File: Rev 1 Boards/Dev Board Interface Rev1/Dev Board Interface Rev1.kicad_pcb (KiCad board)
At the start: 2 copper layers, 53 x 45 mm, 25 parts, among them J1 Conn_01x02_Pin, J2 Conn_01x02_Pin, J3 Conn_01x04_Pin, U1 TLV9301xDBV, U2 ADS1014IDGS, U3 ADS1014IDGS, U4 ISO164xB, U5 DACx53401

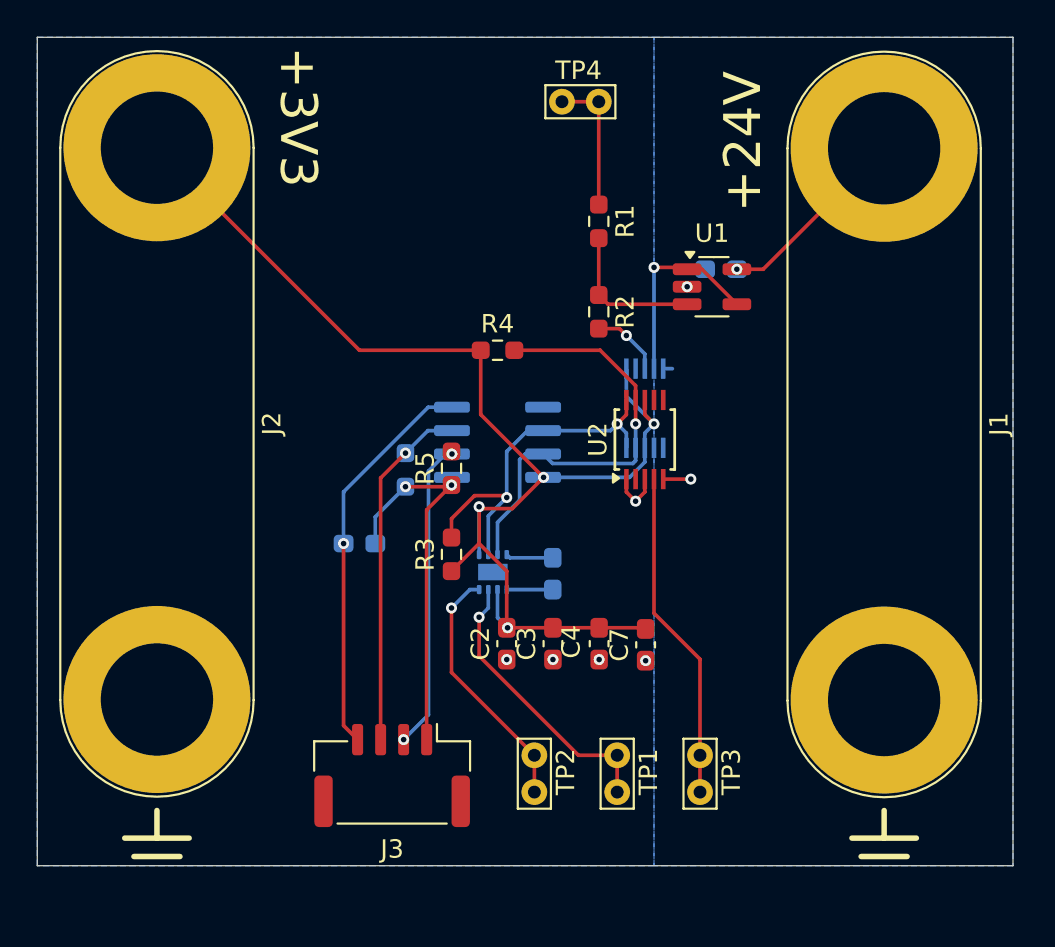
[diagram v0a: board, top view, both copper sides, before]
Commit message: implemented dev board interface review suggestions as per morris
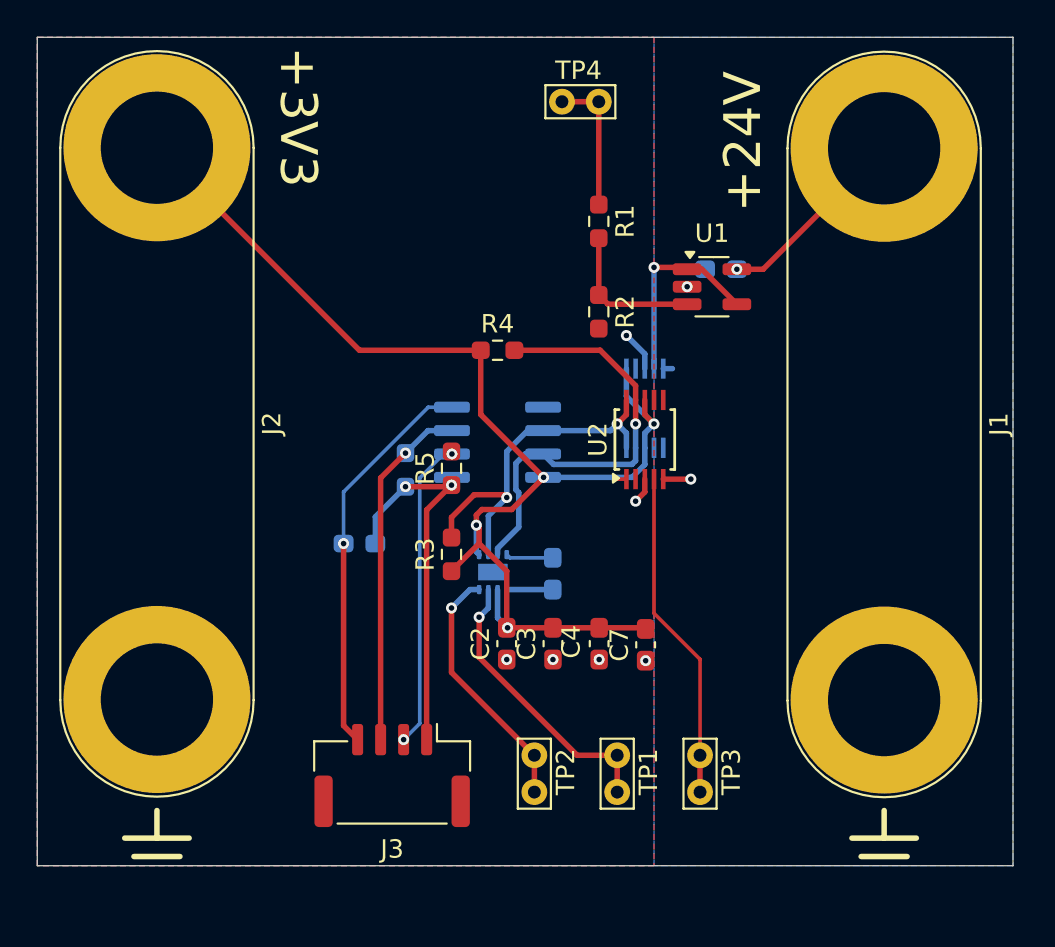
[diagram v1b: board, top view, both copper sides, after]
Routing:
- net GND: track 9.18 -> 6.62 mm
- net +3V3: track 69.9 -> 68.9 mm
- added copper zone on F.Cu, net GND

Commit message: Did partial fixes according to round 2 review of dev board interface as per jed
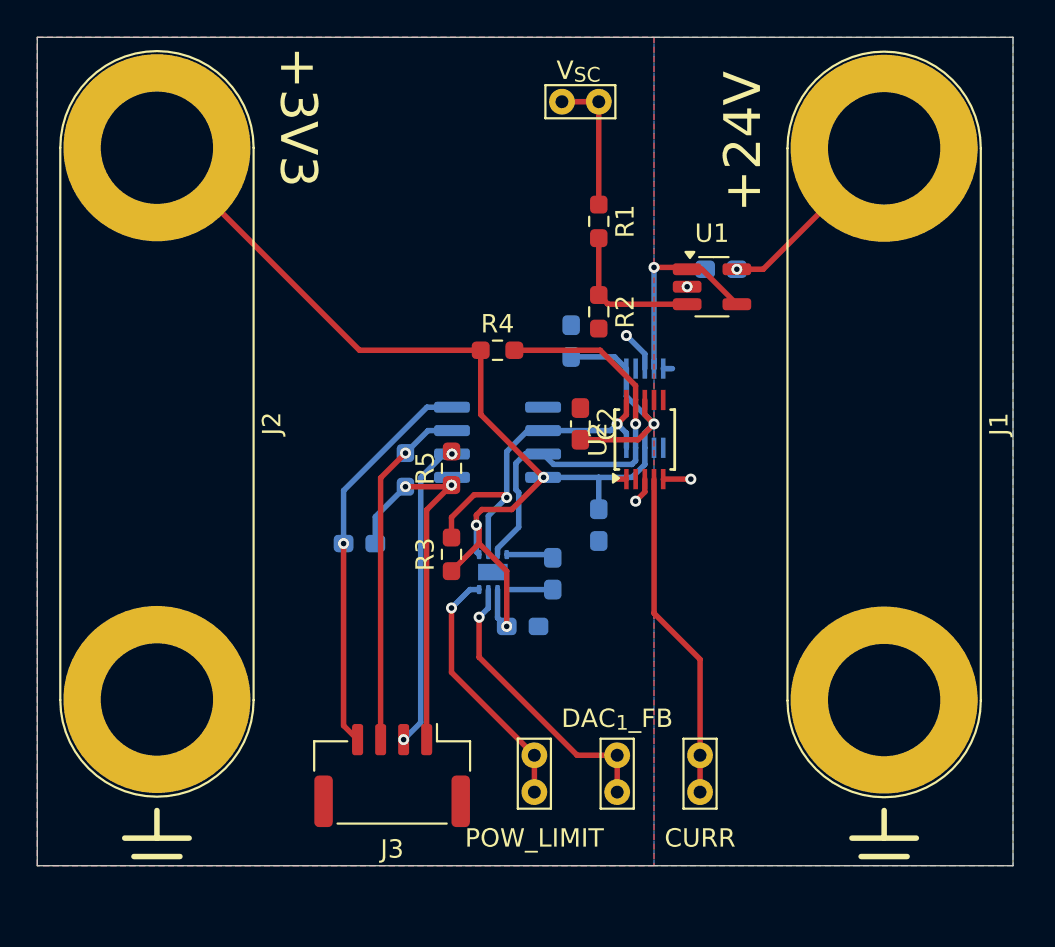
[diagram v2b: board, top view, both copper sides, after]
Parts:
- C3, C4, C7: moved to B.Cu
- moved C3 16.5 mm to (80.0, 106.0), turned to -90 degrees
- moved C2 12.6 mm to (80.5, 110.5), turned to -90 degrees
- moved C7 6.76 mm to (77.4, 121.5), turned to 180 degrees
- moved C4 6.44 mm to (81.5, 116.0)
- renumbered TP3 to CURR, TP1 to DAC_{1}_FB, TP2 to POW_LIMIT, TP4 to V_{SC}
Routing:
- net +3V3: track 68.9 -> 70.5 mm
- net GND: vias 6 -> 2

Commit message: reworked dev board interface pcb layout to put all ICs on the same side as  per jed review
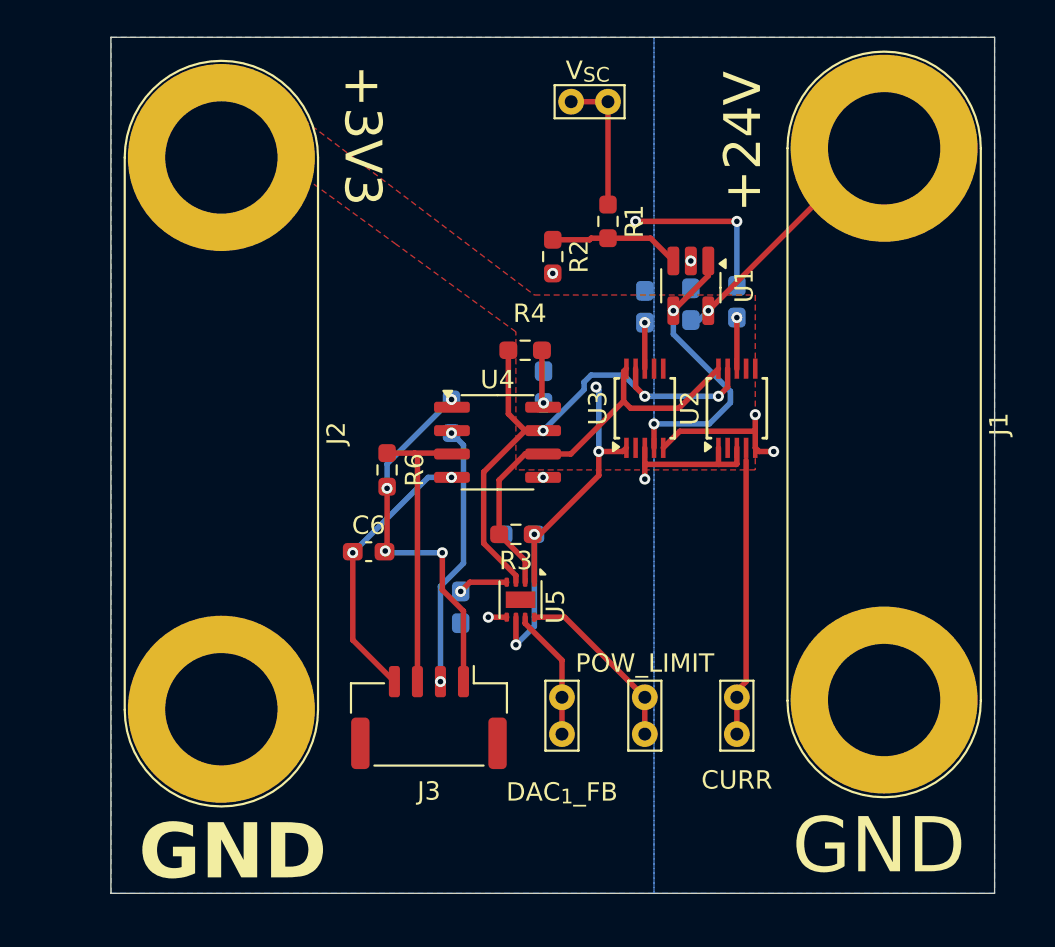
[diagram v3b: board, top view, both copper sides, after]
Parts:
- C2, R5: moved to B.Cu
- C6, R6, U3, U4, U5: moved to F.Cu
- moved C2 10.8 mm to (89.0, 103.9)
- moved C4 8.08 mm to (78.5, 108.5), turned to 90 degrees
- moved POW_LIMIT 6.78 mm to (84.0, 127.3)
- moved C5 5.32 mm to (74.0, 120.5)
- moved U2 5.28 mm to (89.0, 109.7)
- moved C7 5.01 mm to (77.1, 116.5), turned to 0 degrees
- moved C3 4.41 mm to (84.0, 104.1)
- moved DAC_{1}_FB 4.35 mm to (79.5, 127.3)
- moved R2 3.91 mm to (79.0, 101.4)
- moved CURR 3.73 mm to (89.0, 127.3)
- moved J3 3.73 mm to (72.3, 126.5)
- moved R3 3.67 mm to (77.0, 116.5), turned to 180 degrees
- moved J2 3.54 mm to (61.0, 96.0)
- moved R5 2.82 mm to (73.5, 110.1), turned to -90 degrees
- moved C1 2.51 mm to (86.5, 104.0), turned to -90 degrees
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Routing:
- net +3V3: track 70.5 -> 30.3 mm, vias 4 -> 7
- net GND: track 6.62 -> 18.5 mm, vias 2 -> 6
- net /DAC_{1}_FB: track 15.6 -> 7.18 mm, vias 1 -> 0
- net GNDD: track 21.6 -> 15.1 mm, vias 1 -> 2
- net /Dev Board Interface/SDA_{INT}: track 24.0 -> 30.5 mm, vias 1 -> 3
- net GNDPWR: track 2.00 -> 8.27 mm, vias 2 -> 3
- net /Dev Board Interface/V_{SC}_BUF: track 10.8 -> 15.7 mm, vias 1 -> 2
- net /POW_LIMIT: track 13.8 -> 9.80 mm, vias 1 -> 0
- net +24V: track 10.7 -> 14.4 mm
- net /SCL_{IN}: track 19.2 -> 16.0 mm, vias 1 -> 0
- net /CURR: track 18.0 -> 15.1 mm
- net /SDA_{IN}: track 16.8 -> 14.4 mm
- net /Dev Board Interface/SCL_{INT}: track 20.3 -> 22.7 mm, vias 2 -> 0
- net /Dev Board Interface/V_{SC}_scaled: track 8.09 -> 7.10 mm
- net /+3V3_{DEV}: track 21.1 -> 20.9 mm, vias 2 -> 4
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- added copper zone on F.Cu, net +3V3
- removed copper zone on F.Cu, net GND
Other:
- board size 53 x 45 mm -> 48 x 46.5 mm
- board text added: "GND"
